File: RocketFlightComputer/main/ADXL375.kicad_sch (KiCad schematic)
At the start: 4 parts

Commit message: Corrections of mistake, revision of schematic is done and BOM revised, revision of pcb layout to do
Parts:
- C37: LCSC C48579250 -> C1590
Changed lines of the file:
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@@
 			)
 		)
-		(property "LCSC" "C48579250"
+		(property "LCSC" "C1590"
 			(at 49.53 58.42 0)
 			(hide yes)

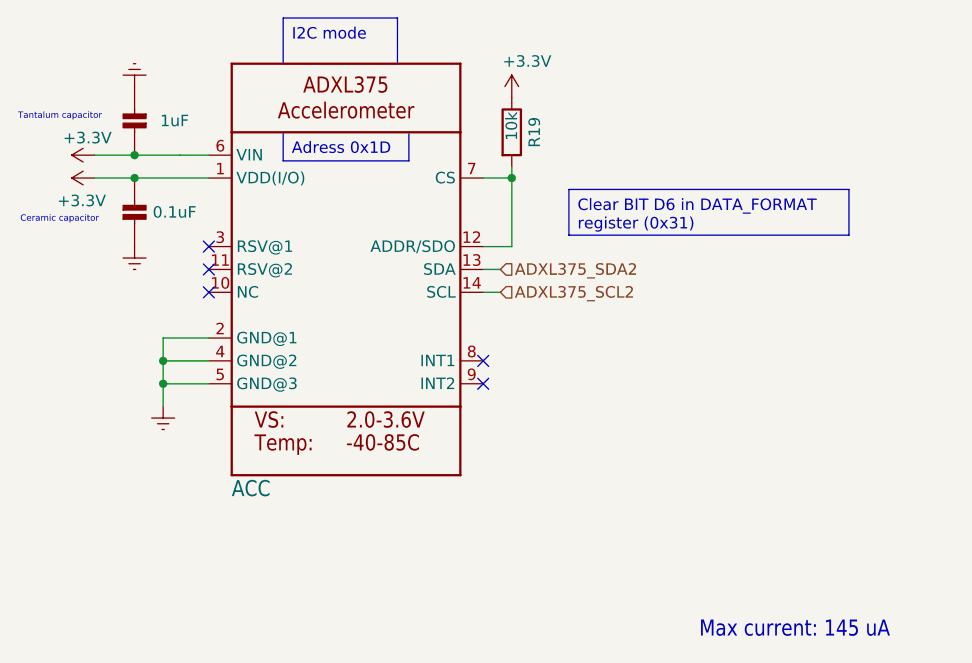
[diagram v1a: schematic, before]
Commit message: Was missing pull ups on adxl375
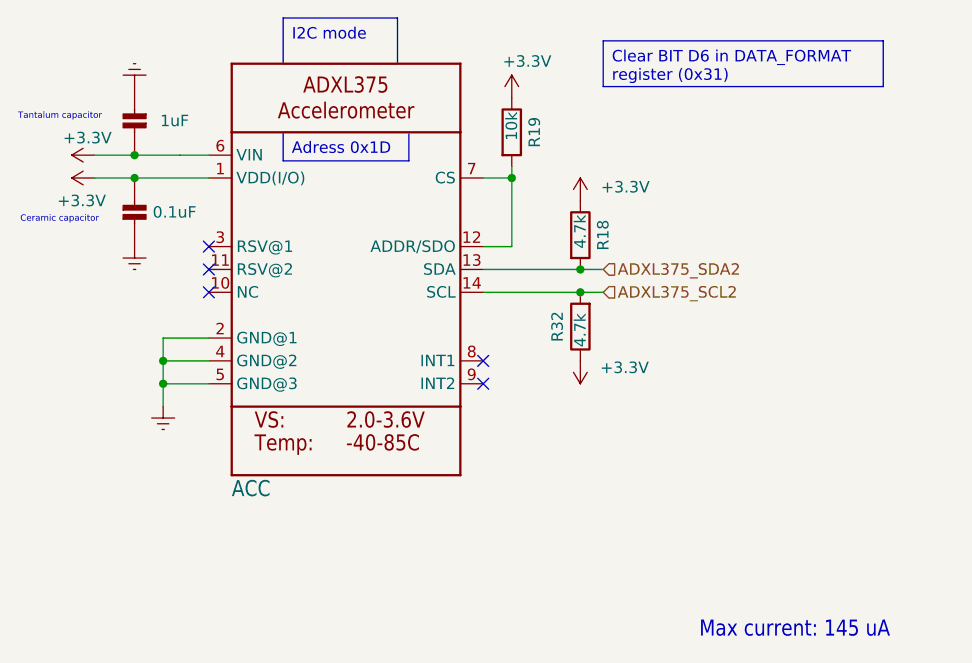
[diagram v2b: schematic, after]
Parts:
- added R18, R32: 4.7k, Resistor_SMD:R_0603_1608Metric_Pad0.98x0.95mm_HandSolder, symbol Device:R
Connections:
- net +3.3V: now also R18.1, R32.1
- net ADXL375_SCL2: now also R32.2
- net ADXL375_SDA2: now also R18.2
